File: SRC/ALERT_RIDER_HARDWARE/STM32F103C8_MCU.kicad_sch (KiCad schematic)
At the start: 33 parts, among them J8 Conn_01x06, SW1 reset, SW2 GREEN, SW3 YELLOW, SW4 RED, SW5 CHANNEL, U2 STM32F103C8Tx, U6 SM420561N, Y1 8MHz, Y2 32.678KHz

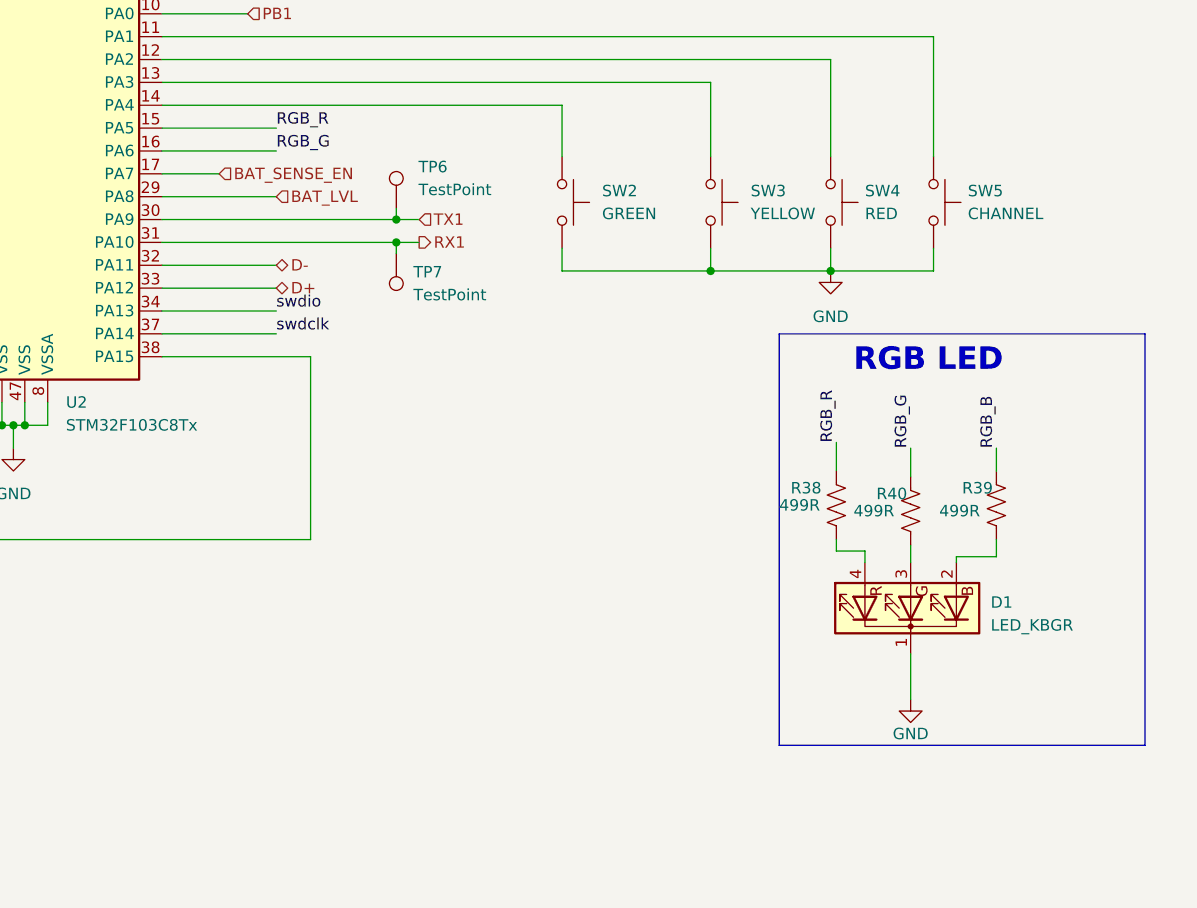
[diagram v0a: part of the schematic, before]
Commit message: complete Pa8-Pa7 LED placement maximized all files generated
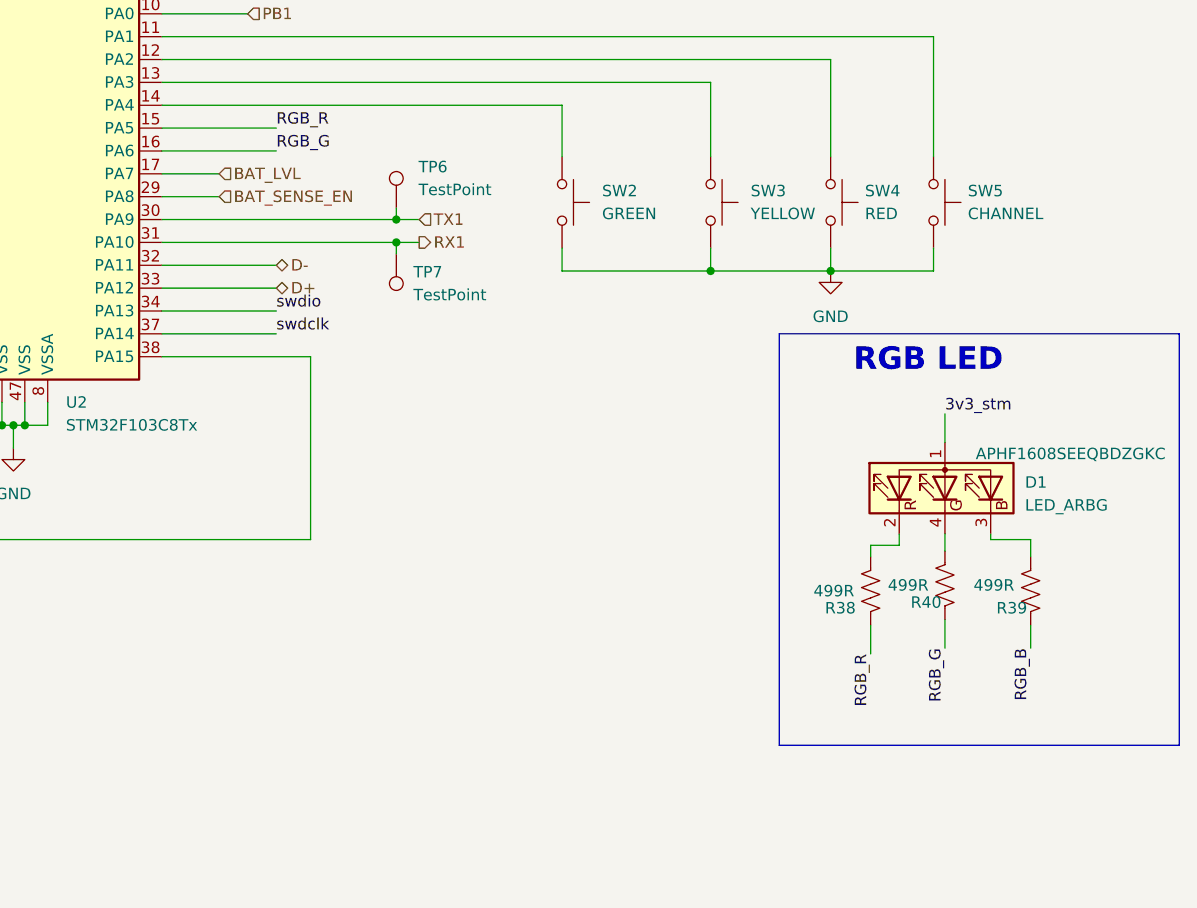
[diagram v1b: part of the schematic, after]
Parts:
- removed D1: LED_KBGR, MACHADA_footprints:RCG_LED_606_TJ-S1615CY6TGLCCSRGB-A5, symbol Device:LED_KBGR
- added D1: LED_ARBG, MACHADA_footprints:LED_APHF1608SEEQBDZGKC, symbol Device:LED_ARBG
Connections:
- net 3v3_stm: now also D1.1 (A)
- net BAT_LVL: now also U2.17 (PA7); no longer U2.29 (PA8)
- net BAT_SENSE_EN: now also U2.29 (PA8); no longer U2.17 (PA7)
- net at R38.2: now also D1.2 (RK)
- net at R40.2: now also D1.4 (GK)
- net at R39.2: now also D1.3 (BK)
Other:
- moved on the sheet: R38, R39, R40

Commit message: complete update on production files and Design files
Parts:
- removed C11, C12, C13, C14: 22p, Capacitor_SMD:C_0402_1005Metric, symbol Device:C_Small
- removed R7: 1M, Resistor_SMD:R_0402_1005Metric, symbol Device:R_US
- removed Y1: 8MHz, Crystal:Crystal_SMD_3225-4Pin_3.2x2.5mm, symbol Device:Crystal_GND24
- removed Y2: 32.678KHz, Crystal:Crystal_SMD_3215-2Pin_3.2x1.5mm, symbol Device:Crystal
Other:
- note removed: "HSE OSCILLATOR"
- note removed: "LPE OSCILLATOR"
